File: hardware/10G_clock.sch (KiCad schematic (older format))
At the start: 12 parts, among them U801 DIFF_OSC, U802 DIFF_OSC, U803 SI53340

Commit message: Layouted USB-UART.
Also moved USB-OTG to the right Side of the Board. To get there
some free Space, i moved the DDR3/Memory and the FPGA a few
Millimeters down.
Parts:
- R801, R802, R803, R804: footprint Resistors_SMD:R_0402 -> Resistor_SMD:R_0402_1005Metric
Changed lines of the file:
@@
 F 0 "R804" V 3780 4050 50  0000 C CNN
 F 1 "100" V 3700 4050 50  0000 C CNN
-F 2 "Resistors_SMD:R_0402" V 3630 4050 50  0001 C CNN
+F 2 "Resistor_SMD:R_0402_1005Metric" V 3630 4050 50  0001 C CNN
 F 3 "" H 3700 4050 50  0000 C CNN
 	1    3700 4050
@@
 F 0 "R801" V 2580 4400 50  0000 C CNN
 F 1 "0" V 2500 4400 50  0000 C CNN
-F 2 "Resistors_SMD:R_0402" V 2430 4400 50  0001 C CNN
+F 2 "Resistor_SMD:R_0402_1005Metric" V 2430 4400 50  0001 C CNN
 F 3 "" H 2500 4400 50  0000 C CNN
 	1    2500 4400
@@
 F 0 "R803" V 2880 4500 50  0000 C CNN
 F 1 "0" V 2800 4500 50  0000 C CNN
-F 2 "Resistors_SMD:R_0402" V 2730 4500 50  0001 C CNN
+F 2 "Resistor_SMD:R_0402_1005Metric" V 2730 4500 50  0001 C CNN
 F 3 "" H 2800 4500 50  0000 C CNN
 	1    2800 4500
@@
 F 0 "R802" V 2580 4700 50  0000 C CNN
 F 1 "0" V 2500 4700 50  0000 C CNN
-F 2 "Resistors_SMD:R_0402" V 2430 4700 50  0001 C CNN
+F 2 "Resistor_SMD:R_0402_1005Metric" V 2430 4700 50  0001 C CNN
 F 3 "" H 2500 4700 50  0000 C CNN
 	1    2500 4700

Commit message: Improved Powerdistribution Network of the FPGA.
Also started to layout USB.
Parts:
- C801, C802, C803, C804, C805: footprint Capacitors_SMD:C_0402 -> Capacitor_SMD:C_0402_1005Metric
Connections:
- wire segments 25 -> 31
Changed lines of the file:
@@
 F 0 "C803" H 3510 3970 50  0000 L CNN
 F 1 "100n" H 3510 3820 50  0000 L CNN
-F 2 "Capacitors_SMD:C_0402" H 3500 3900 50  0001 C CNN
+F 2 "Capacitor_SMD:C_0402_1005Metric" H 3500 3900 50  0001 C CNN
 F 3 "" H 3500 3900 50  0000 C CNN
 	1    3500 3900
@@
 F 0 "C804" H 3510 4270 50  0000 L CNN
 F 1 "100n" H 3510 4120 50  0000 L CNN
-F 2 "Capacitors_SMD:C_0402" H 3500 4200 50  0001 C CNN
+F 2 "Capacitor_SMD:C_0402_1005Metric" H 3500 4200 50  0001 C CNN
 F 3 "" H 3500 4200 50  0000 C CNN
 	1    3500 4200
@@
 $EndComp
 Wire Wire Line
-	3600 3900 3900 3900
-Wire Wire Line
-	3600 4200 3900 4200
+	3600 3900 3700 3900
+Wire Wire Line
+	3600 4200 3700 4200
 Connection ~ 3700 3900
 Connection ~ 3700 4200
@@
 F 0 "C802" H 3375 3350 50  0000 L CNN
 F 1 "100n" H 3375 3150 50  0000 L CNN
-F 2 "Capacitors_SMD:C_0402" H 3388 3100 50  0001 C CNN
+F 2 "Capacitor_SMD:C_0402_1005Metric" H 3388 3100 50  0001 C CNN
 F 3 "" H 3350 3250 50  0000 C CNN
 	1    3350 3250
@@
 $EndComp
 Wire Wire Line
-	3200 3500 3200 3000
+	3200 3500 3200 3100
 Wire Wire Line
 	3200 3100 3350 3100
@@
 F 0 "C805" H 4925 3400 50  0000 L CNN
 F 1 "1u" H 4925 3200 50  0000 L CNN
-F 2 "Capacitors_SMD:C_0402" H 4938 3150 50  0001 C CNN
+F 2 "Capacitor_SMD:C_0402_1005Metric" H 4938 3150 50  0001 C CNN
 F 3 "" H 4900 3300 50  0000 C CNN
 	1    4900 3300
@@
 $EndComp
 Wire Wire Line
-	4700 3500 4700 3050
+	4700 3500 4700 3150
 Wire Wire Line
 	4700 3150 4900 3150
@@
 F 0 "C801" H 3375 1650 50  0000 L CNN
 F 1 "100n" H 3375 1450 50  0000 L CNN
-F 2 "Capacitors_SMD:C_0402" H 3388 1400 50  0001 C CNN
+F 2 "Capacitor_SMD:C_0402_1005Metric" H 3388 1400 50  0001 C CNN
 F 3 "" H 3350 1550 50  0000 C CNN
 	1    3350 1550
@@
 	3200 1400 3350 1400
 Wire Wire Line
-	3200 1800 3200 1300
+	3200 1800 3200 1400
 Connection ~ 3200 1400
 $Comp
@@
 	4700 5100 4700 5150
 Wire Wire Line
-	4700 5150 4900 5150
+	4700 5150 4800 5150
 Wire Wire Line
 	4900 5150 4900 5100
@@
 Wire Wire Line
 	2150 4500 2650 4500
+Wire Wire Line
+	3700 3900 3900 3900
+Wire Wire Line
+	3700 4200 3900 4200
+Wire Wire Line
+	3200 3100 3200 3000
+Wire Wire Line
+	4700 3150 4700 3050
+Wire Wire Line
+	3200 1400 3200 1300
+Wire Wire Line
+	4800 5150 4900 5150
 $EndSCHEMATC

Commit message: Fixed Schematic Symbols
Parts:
- C801, C802, C805: symbol device:C -> Device:C_Small
- C803, C804: symbol device:C_Small -> Device:C_Small
- R801, R802, R803, R804: symbol device:R -> Device:R
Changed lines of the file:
@@
 $Descr A4 11693 8268
 encoding utf-8
-Sheet 8 22
+Sheet 8 21
 Title ""
 Date ""
@@
 Note: clocks are AC-coupled at receiving device.
 $Comp
-L power1:GND #PWR084
+L power:GND #PWR084
 U 1 1 598A8A47
 P 1700 2300
@@
 NoConn ~ 5500 4800
 $Comp
-L device:C_Small C803
+L Device:C_Small C803
 U 1 1 598F26F6
 P 3500 3900
@@
 $EndComp
 $Comp
-L device:C_Small C804
+L Device:C_Small C804
 U 1 1 598F2737
 P 3500 4200
@@
 $EndComp
 $Comp
-L device:R R804
+L Device:R R804
 U 1 1 598F277A
 P 3700 4050
@@
 Connection ~ 3700 4200
 $Comp
-L device:C C802
+L Device:C_Small C802
 U 1 1 598F29AD
 P 3350 3250
@@
 $EndComp
 $Comp
-L power1:GND #PWR085
+L power:GND #PWR085
 U 1 1 598F2A12
 P 3350 3400
@@
 $EndComp
 $Comp
-L power1:+3V3 #PWR086
+L power:+3V3 #PWR086
 U 1 1 598F2A6C
 P 3200 3000
@@
 	3300 4200 3400 4200
 $Comp
-L device:C C805
+L Device:C_Small C805
 U 1 1 598F30AD
 P 4900 3300
@@
 $EndComp
 $Comp
-L power1:GND #PWR087
+L power:GND #PWR087
 U 1 1 598F3107
 P 4900 3450
@@
 $EndComp
 $Comp
-L power1:+3V3 #PWR088
+L power:+3V3 #PWR088
 U 1 1 598F312D
 P 4700 3050
@@
 Connection ~ 4700 3150
 $Comp
-L device:C C801
+L Device:C_Small C801
 U 1 1 598F396E
 P 3350 1550
@@
 $EndComp
 $Comp
-L power1:GND #PWR089
+L power:GND #PWR089
 U 1 1 598F3974
 P 3350 1700
@@
 $EndComp
 $Comp
-L power1:+3V3 #PWR090
+L power:+3V3 #PWR090
 U 1 1 598F397A
 P 3200 1300
@@
 Connection ~ 3200 1400
 $Comp
-L power1:GND #PWR091
+L power:GND #PWR091
 U 1 1 598F433B
 P 1700 4000
@@
 NoConn ~ 1800 3500
 $Comp
-L power1:GND #PWR092
+L power:GND #PWR092
 U 1 1 598F54B6
 P 4800 5200
@@
 	3900 3900 3900 4100
 $Comp
-L power1:GND #PWR093
+L power:GND #PWR093
 U 1 1 598F5D66
 P 2350 4400
@@
 $EndComp
 $Comp
-L power1:+3V3 #PWR094
+L power:+3V3 #PWR094
 U 1 1 598F5D8C
 P 2150 4500
@@
 $EndComp
 $Comp
-L power1:GND #PWR095
+L power:GND #PWR095
 U 1 1 598F5DE1
 P 2350 4700
@@
 $EndComp
 $Comp
-L device:R R801
+L Device:R R801
 U 1 1 598F6241
 P 2500 4400
@@
 $EndComp
 $Comp
-L device:R R803
+L Device:R R803
 U 1 1 598F6296
 P 2800 4500
@@
 $EndComp
 $Comp
-L device:R R802
+L Device:R R802
 U 1 1 598F62E9
 P 2500 4700

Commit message: WIP: TLK Powerdistribution
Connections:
- wire segments 31 -> 37
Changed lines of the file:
@@
 EESchema Schematic File Version 4
-LIBS:zynq_board-cache
 EELAYER 26 0
 EELAYER END
 $Descr A4 11693 8268
 encoding utf-8
-Sheet 8 21
+Sheet 7 21
 Title ""
 Date ""
@@
 Wire Wire Line
 	4800 5150 4900 5150
+Wire Wire Line
+	3350 1400 3350 1450
+Wire Wire Line
+	3350 1650 3350 1700
+Wire Wire Line
+	3350 3150 3350 3100
+Wire Wire Line
+	3350 3350 3350 3400
+Wire Wire Line
+	4900 3200 4900 3150
+Wire Wire Line
+	4900 3400 4900 3450
 $EndSCHEMATC

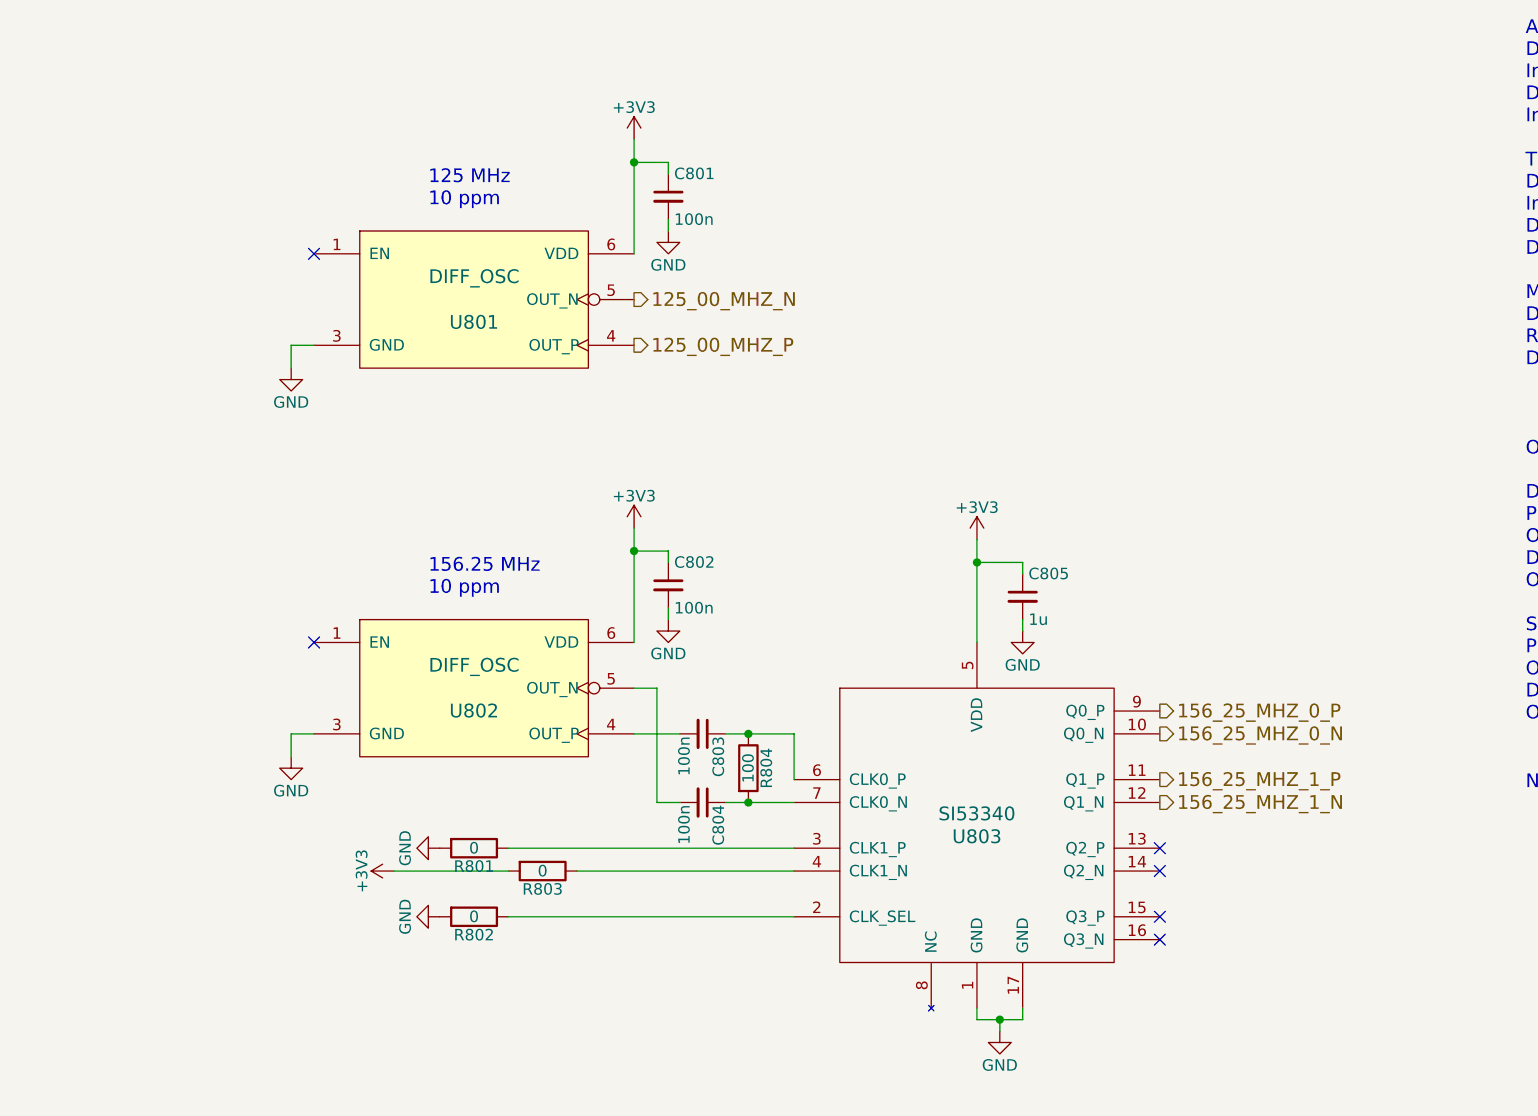
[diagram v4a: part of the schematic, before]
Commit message: SFP+ Power Filter, Levelshifter and MGT/TLK Clock Distribution.
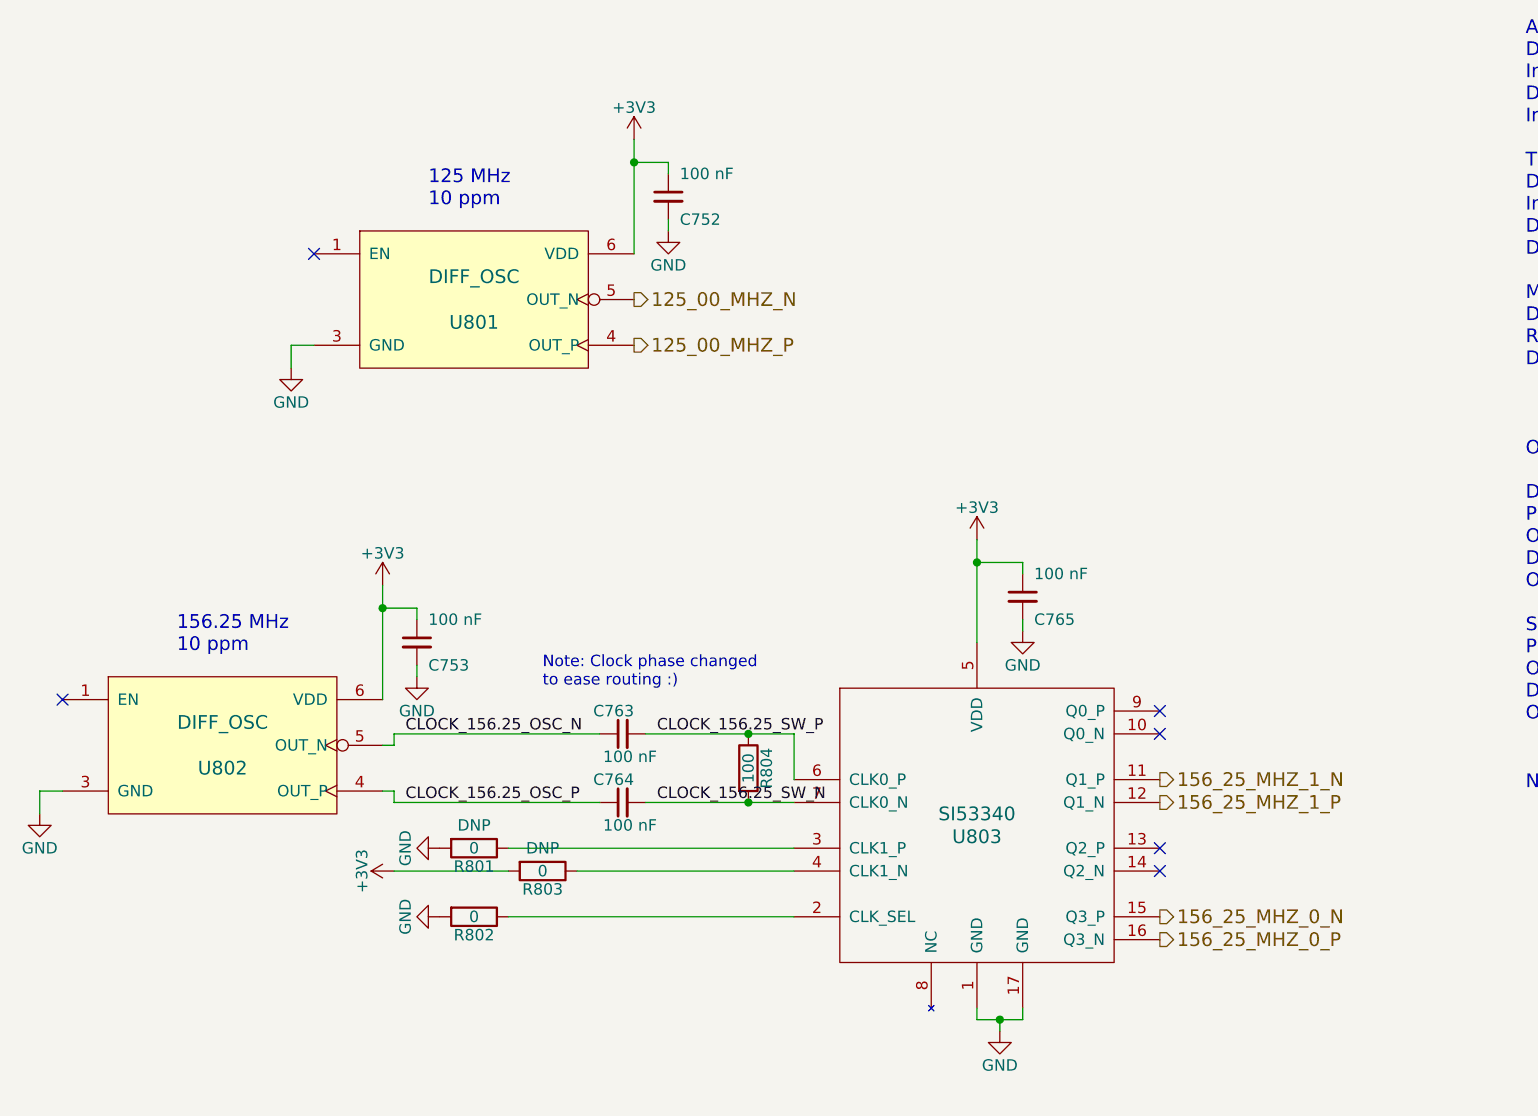
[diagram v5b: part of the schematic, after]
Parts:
- removed C801, C802, C803, C804: 100n, Capacitor_SMD:C_0402_1005Metric, symbol Device:C_Small
- removed C805: 1u, Capacitor_SMD:C_0402_1005Metric, symbol Device:C_Small
- added C752, C753, C763, C764, C765: 100 nF, Capacitor_SMD:C_0201_0603Metric, symbol Device:C_Small
- R801, R803: Populate for CLG484(Z-7012s/Z-7015) (none) -> 1; Populate for SBGA485(Z-7030) (none) -> 1; Populated (none) -> DNP; Source (none) -> SPEC
- U801, U802: footprint footprints:VDFN_3.2x2.5mm -> footprints:Microchip_VDFN_3.2x2.5mm; Populate for CLG484(Z-7012s/Z-7015) (none) -> 1; Populate for SBGA485(Z-7030) (none) -> 1
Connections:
- net +3V3: now also C752.1, C753.1, C765.1
- net 156_25_MHZ_0_N: now also U803.15 (Q3_P); no longer U803.10 (Q0_N)
- net 156_25_MHZ_0_P: now also U803.16 (Q3_N); no longer U803.9 (Q0_P)
- net 156_25_MHZ_1_N: now also U803.11 (Q1_P); no longer U803.12 (Q1_N)
- net 156_25_MHZ_1_P: now also U803.12 (Q1_N); no longer U803.11 (Q1_P)
- net GND: now also C752.2, C753.2, C765.2
- net CLOCK_156.25_OSC_P: now reaches U802.4 (OUT_P)
- net CLOCK_156.25_OSC_P: now also C764.1
- net CLOCK_156.25_OSC_N: now reaches U802.5 (OUT_N)
- net CLOCK_156.25_OSC_N: now also C763.1
- net CLOCK_156.25_SW_P: now reaches R804.1, U803.6 (CLK0_P)
- net CLOCK_156.25_SW_P: now also C763.2
- net CLOCK_156.25_SW_N: now reaches R804.2, U803.7 (CLK0_N)
- net CLOCK_156.25_SW_N: now also C764.2
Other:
- note added: "Note: Clock phase changed\nto ease routing :)"
- moved on the sheet: U802

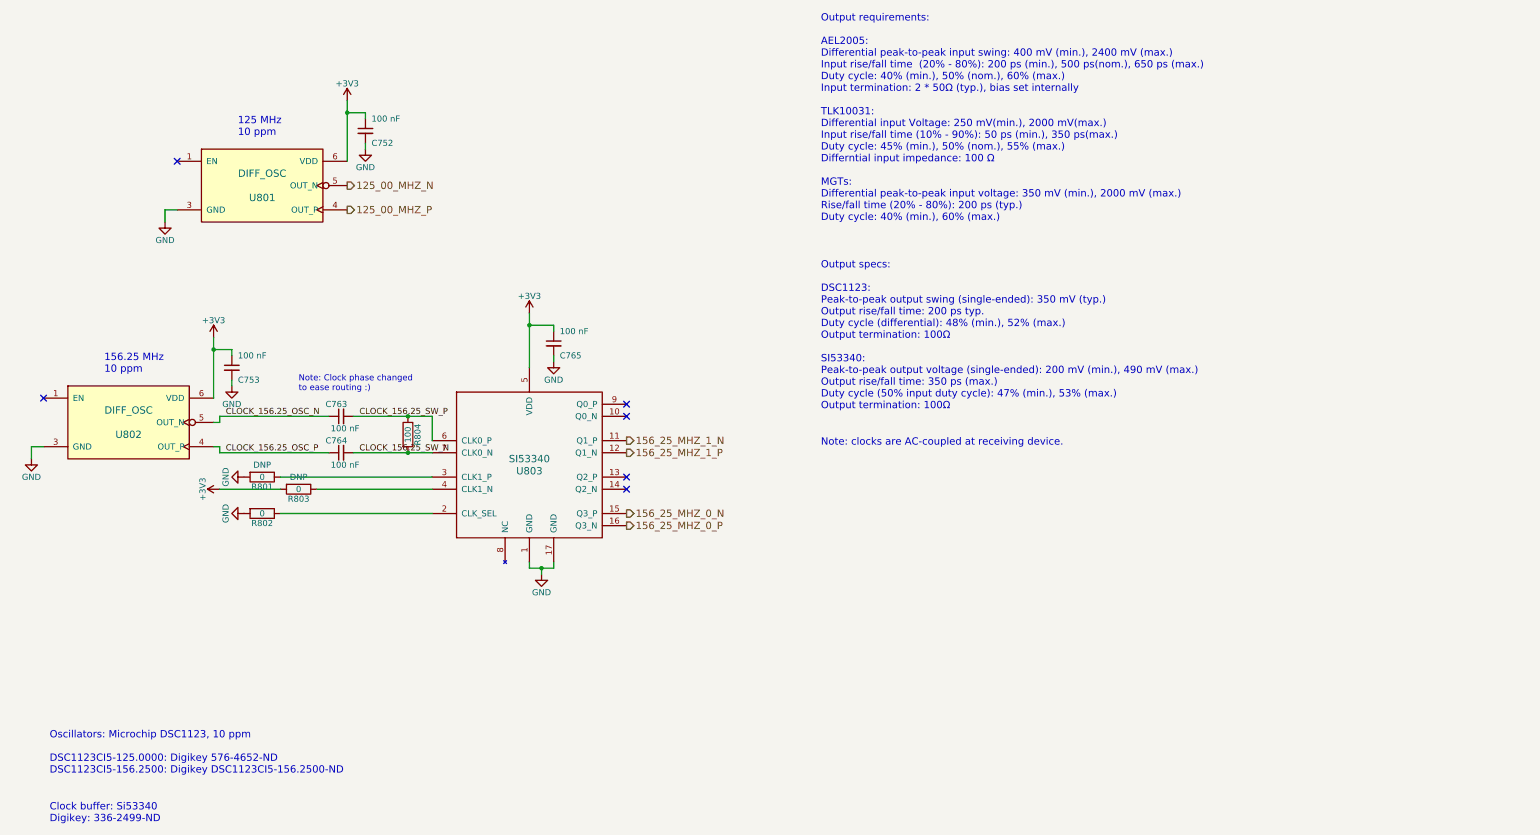
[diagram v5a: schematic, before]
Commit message: PS Clock, Reset Button, Cam Levelshifters and big 1.0 V Cap placed.
Improved some Footprints and library Symbols.

Also though about Chassis Ground.
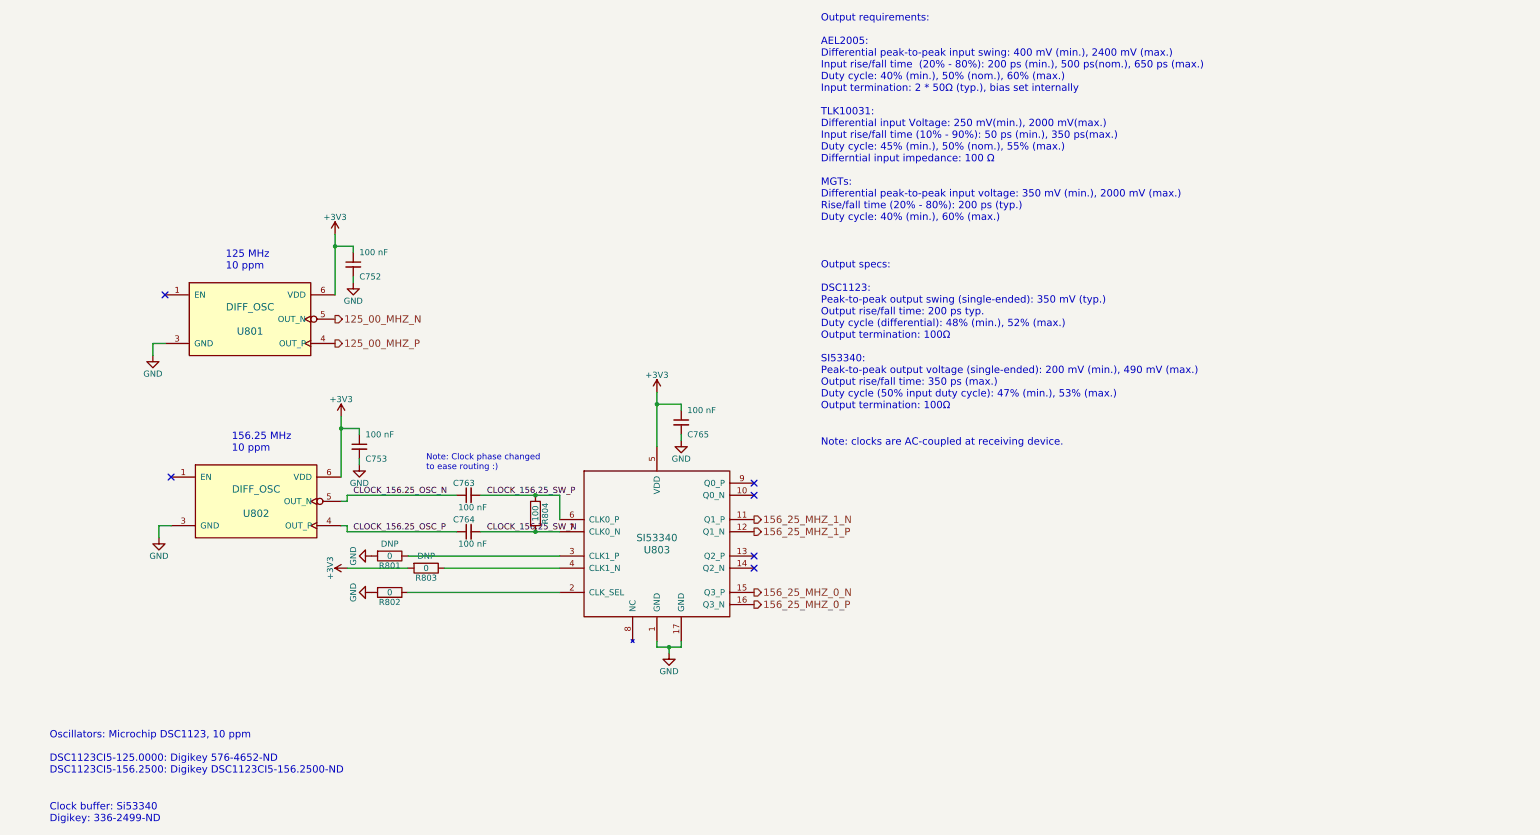
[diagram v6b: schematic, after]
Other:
- moved on the sheet: C752, C753, C763, C764, C765, R801, R802, R803, R804, U801, U802, U803
